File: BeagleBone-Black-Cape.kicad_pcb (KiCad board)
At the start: 4 copper layers, 61.9 x 92.1 mm, 77 parts, among them J501 Conn_ARM_JTAG_SWD_10, J502 3.3V, P101 BeagleBone_Black_Header, P102 BeagleBone_Black_Header, U401 LM3671, U601 cc1352p, U602 MX25R8035FZUIL0, Y601 32.768kHz, Y602 48MHz

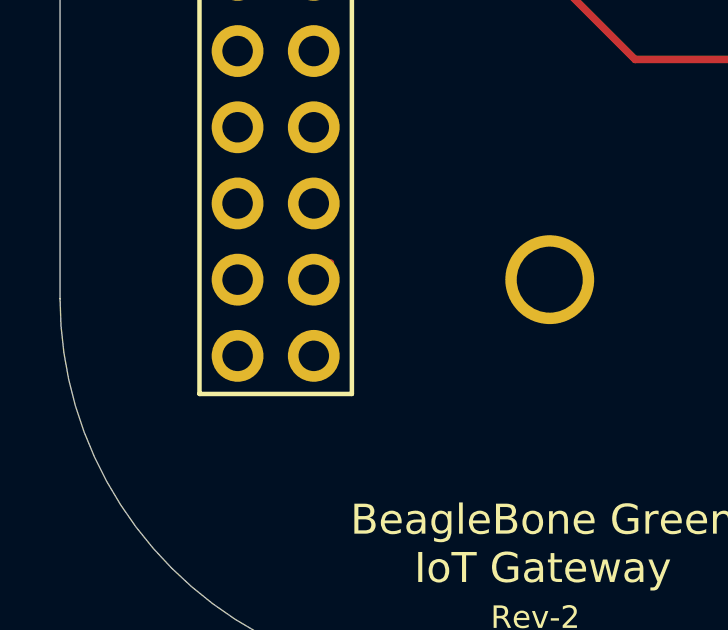
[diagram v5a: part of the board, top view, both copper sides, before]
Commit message: Connected U.FL ground pins to ground and 2x23 connector ground pins to each other
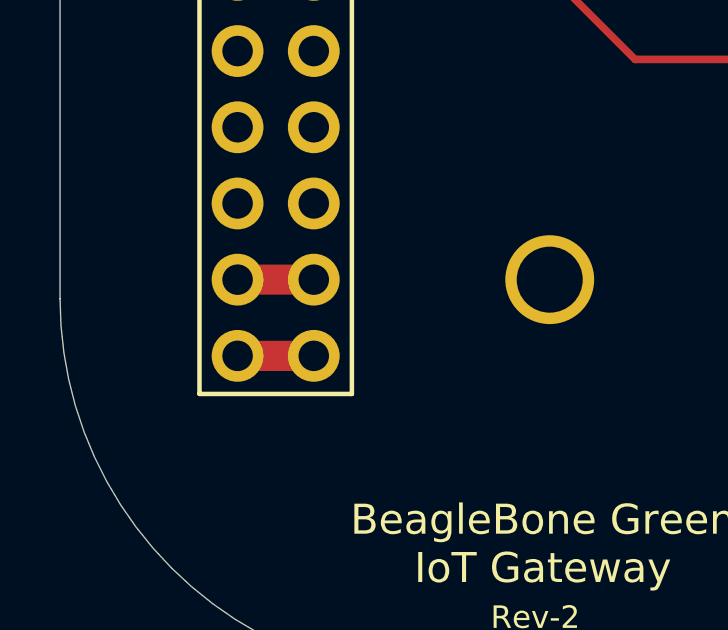
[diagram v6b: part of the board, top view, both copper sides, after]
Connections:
- AE201 pad 2: (no net) -> GND
- AE202 pad 2: (no net) -> GND
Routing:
- net GND: track 160.6 -> 179.0 mm, vias 62 -> 63
- net (no net): track 15.1 -> 1.02 mm, vias 2 -> 1
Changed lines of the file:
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@@
     (thickness 1.6)
     (drawings 22)
-    (tracks 938)
+    (tracks 939)
     (zones 0)
     (modules 77)
@@
   )
   (setup
-    (last_trace_width 0.25)
+    (last_trace_width 1)
     (user_trace_width 0.2)
     (user_trace_width 0.6)
@@
       (effects (font (size 0.6 0.6) (thickness 0.09)))
     )
-    (pad 2 smd rect (at 0.475 -1.475 270) (size 2.2 1.05) (layers F.Cu F.Paste F.Mask))
+    (pad 2 smd rect (at 0.475 -1.475 270) (size 2.2 1.05) (layers F.Cu F.Paste F.Mask)
+      (net 26 GND))
     (pad 1 smd rect (at -1.05 0 270) (size 1.05 1) (layers F.Cu F.Paste F.Mask)
       (net 14 "Net-(AE201-Pad1)"))
-    (pad 2 smd rect (at 0.475 1.475 270) (size 2.2 1.05) (layers F.Cu F.Paste F.Mask))
+    (pad 2 smd rect (at 0.475 1.475 270) (size 2.2 1.05) (layers F.Cu F.Paste F.Mask)
+      (net 26 GND))
     (model ${KISYS3DMOD}/Connector_Coaxial.3dshapes/U.FL_Hirose_U.FL-R-SMT-1_Vertical.wrl
       (offset (xyz 0.4749999928262157 0 0))
@@
       (effects (font (size 0.6 0.6) (thickness 0.09)))
     )
-    (pad 2 smd rect (at 0.475 -1.475 270) (size 2.2 1.05) (layers F.Cu F.Paste F.Mask))
+    (pad 2 smd rect (at 0.475 -1.475 270) (size 2.2 1.05) (layers F.Cu F.Paste F.Mask)
+      (net 26 GND))
     (pad 1 smd rect (at -1.05 0 270) (size 1.05 1) (layers F.Cu F.Paste F.Mask)
       (net 15 "Net-(AE202-Pad1)"))
-    (pad 2 smd rect (at 0.475 1.475 270) (size 2.2 1.05) (layers F.Cu F.Paste F.Mask))
+    (pad 2 smd rect (at 0.475 1.475 270) (size 2.2 1.05) (layers F.Cu F.Paste F.Mask)
+      (net 26 GND))
     (model ${KISYS3DMOD}/Connector_Coaxial.3dshapes/U.FL_Hirose_U.FL-R-SMT-1_Vertical.wrl
       (offset (xyz 0.4749999928262157 0 0))
@@
   (segment (start 129.6201 108.3824) (end 124.6201 103.3824) (width 0.25) (layer F.Cu) (net 25))
   (segment (start 139.9201 106.5324) (end 139.9201 107.9824) (width 0.2) (layer B.Cu) (net 25))
-  (via (at 148.5701 126.6574) (size 2) (drill 1.5) (layers F.Cu B.Cu) (net 0))
-  (segment (start 148.5451 126.6824) (end 148.5701 126.6574) (width 1) (layer F.Cu) (net 0))
-  (segment (start 144.4701 126.6824) (end 148.5451 126.6824) (width 1) (layer F.Cu) (net 0))
-  (segment (start 148.6201 126.7074) (end 148.5701 126.6574) (width 1) (layer F.Cu) (net 0))
-  (segment (start 152.6451 126.7074) (end 148.6201 126.7074) (width 1) (layer F.Cu) (net 0))
-  (segment (start 141.5201 126.6824) (end 144.4701 126.6824) (width 1) (layer F.Cu) (net 0))
-  (segment (start 152.6451 126.7074) (end 155.5951 126.7074) (width 1) (layer F.Cu) (net 0))
+  (via (at 148.5701 126.6574) (size 2) (drill 1.5) (layers F.Cu B.Cu) (net 26))
+  (segment (start 148.5451 126.6824) (end 148.5701 126.6574) (width 1) (layer F.Cu) (net 26))
+  (segment (start 144.4701 126.6824) (end 148.5451 126.6824) (width 1) (layer F.Cu) (net 26))
+  (segment (start 148.6201 126.7074) (end 148.5701 126.6574) (width 1) (layer F.Cu) (net 26))
+  (segment (start 152.6451 126.7074) (end 148.6201 126.7074) (width 1) (layer F.Cu) (net 26))
+  (segment (start 141.5201 126.6824) (end 144.4701 126.6824) (width 1) (layer F.Cu) (net 26))
+  (segment (start 152.6451 126.7074) (end 155.5951 126.7074) (width 1) (layer F.Cu) (net 26))
   (segment (start 136.866753 83.5924) (end 137.4401 83.5924) (width 0.2) (layer F.Cu) (net 8))
   (segment (start 127.8301 83.5924) (end 136.866753 83.5924) (width 0.2) (layer F.Cu) (net 8))
@@
   (via (at 170.2786 58.1269) (size 0.4) (drill 0.3) (layers F.Cu B.Cu) (net 26))
   (via (at 139.9201 83.0324) (size 0.6) (drill 0.4) (layers F.Cu B.Cu) (net 26) (status 30))
-  (segment (start 119.4689 115.1636) (end 118.9101 115.7224) (width 0.25) (layer F.Cu) (net 26) (status 30))
   (segment (start 147.7201 107.7949) (end 147.7326 107.7824) (width 0.2) (layer F.Cu) (net 26) (status 30))
   (segment (start 147.7201 110.0324) (end 147.7201 107.7949) (width 0.2) (layer F.Cu) (net 26) (status 30))
@@
   (segment (start 162.1201 62.3824) (end 161.2201 61.4824) (width 1) (layer F.Cu) (net 26))
   (segment (start 164.6301 62.3824) (end 162.1201 62.3824) (width 1) (layer F.Cu) (net 26))
+  (segment (start 116.3701 115.7224) (end 118.9101 115.7224) (width 1) (layer F.Cu) (net 26))
+  (segment (start 116.3701 118.2624) (end 118.9101 118.2624) (width 1) (layer F.Cu) (net 26))
   (segment (start 138.3251 82.2074) (end 137.4401 83.0924) (width 0.2) (layer B.Cu) (net 152))
   (segment (start 143.872258 82.2074) (end 138.3251 82.2074) (width 0.2) (layer B.Cu) (net 152))

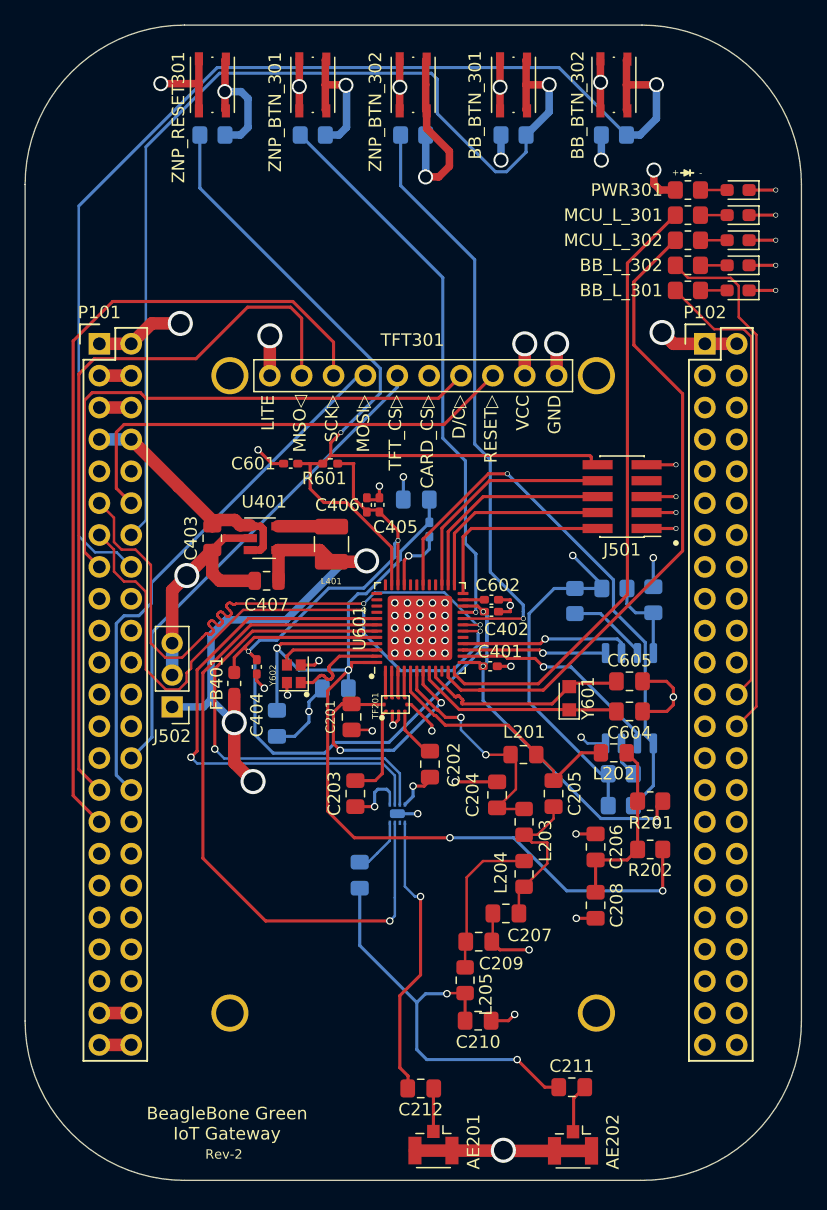
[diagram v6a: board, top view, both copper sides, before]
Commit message: Used PCB cleanup tool w/o the "delete track segments connecting different nets" option (it keeps unlisted pins happy)
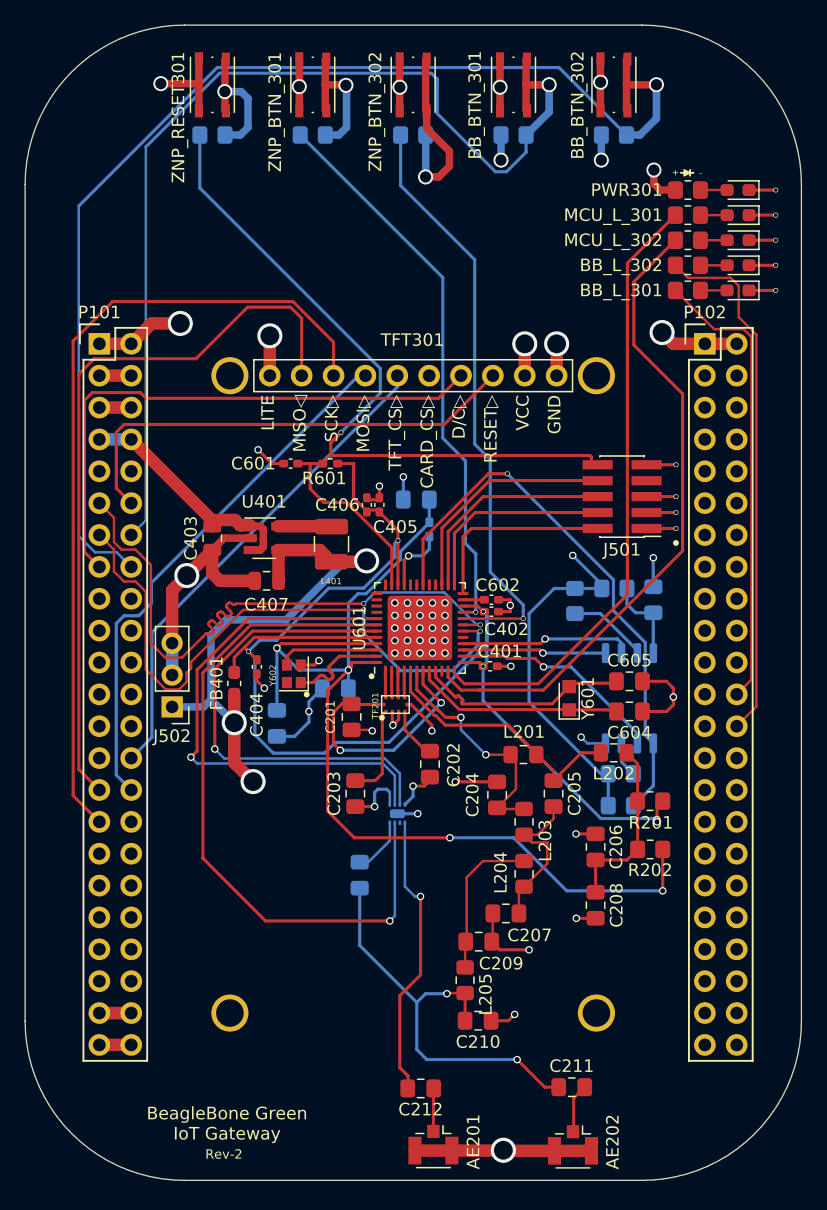
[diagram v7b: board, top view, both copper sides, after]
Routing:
- net (no net): track 1.02 -> 0.00 mm, vias 1 -> 0

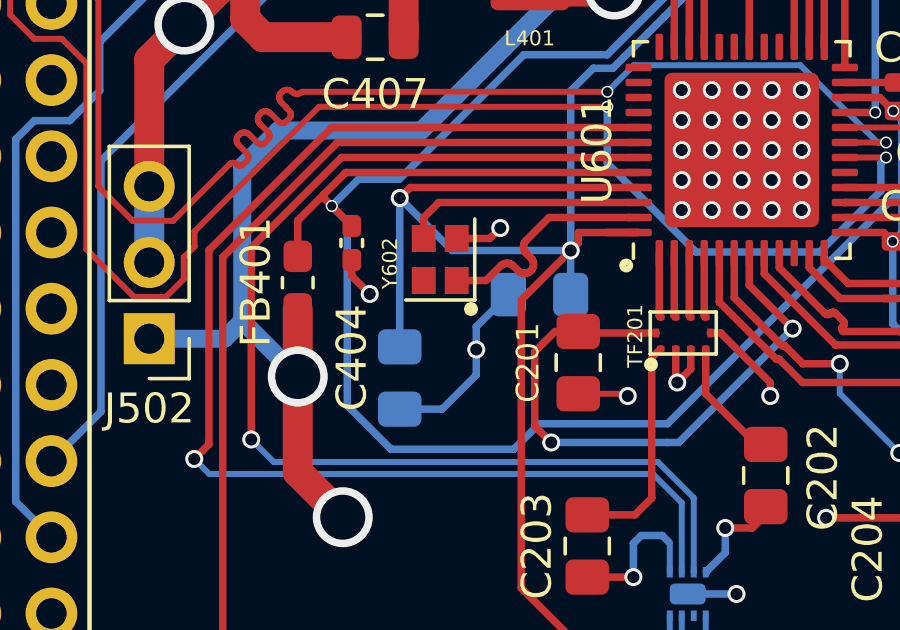
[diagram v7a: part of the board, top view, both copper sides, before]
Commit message: Updated schematic and a symbol so that Y602 pad 4 was connected to the gnd net
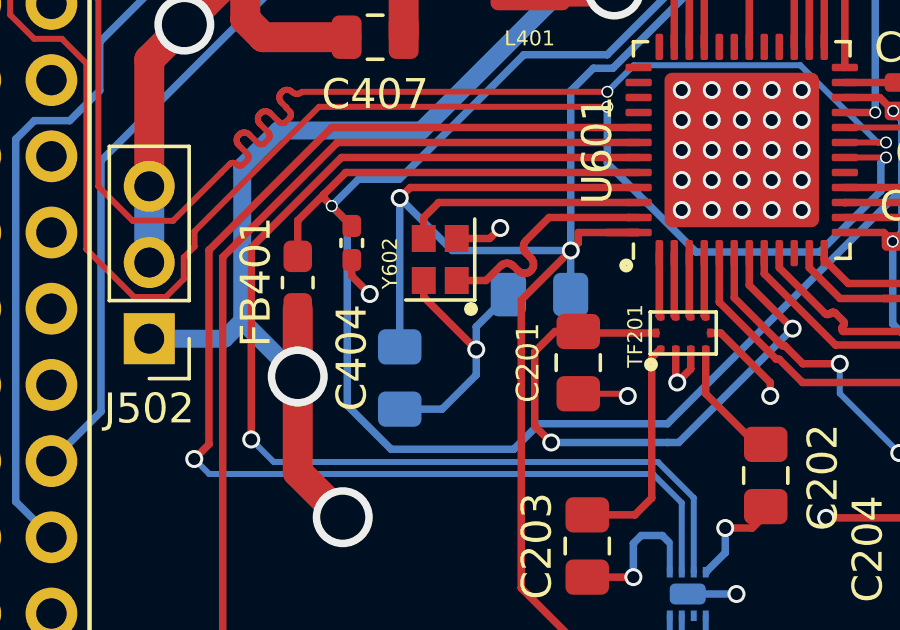
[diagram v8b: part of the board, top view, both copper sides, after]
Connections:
- Y602 pad 4: (no net) -> GND
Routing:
- net GND: track 179.0 -> 182.1 mm
